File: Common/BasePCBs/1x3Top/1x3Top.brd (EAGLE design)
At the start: 100 x 80 mm, 1 part

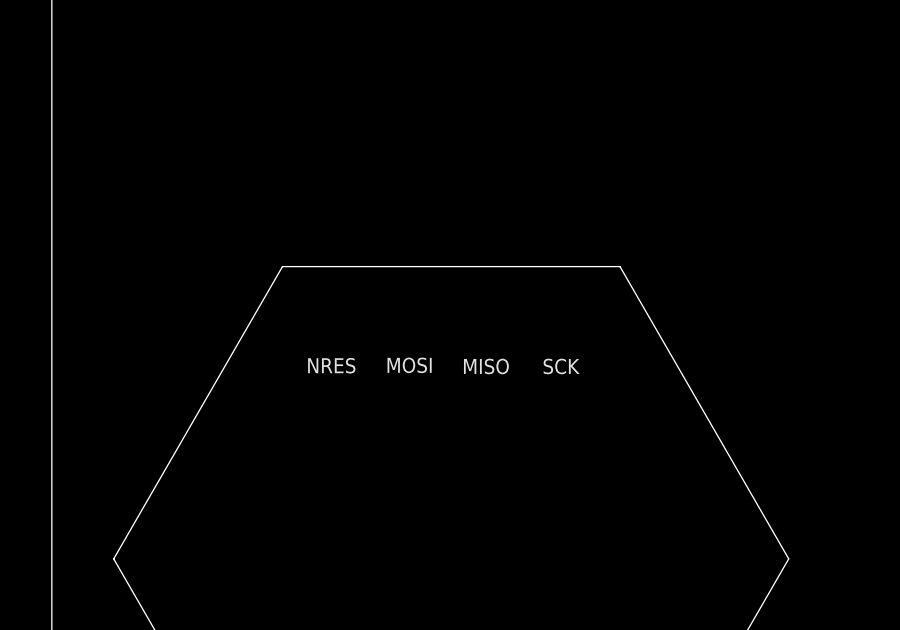
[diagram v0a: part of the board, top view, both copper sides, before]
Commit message: re-organized dimensions
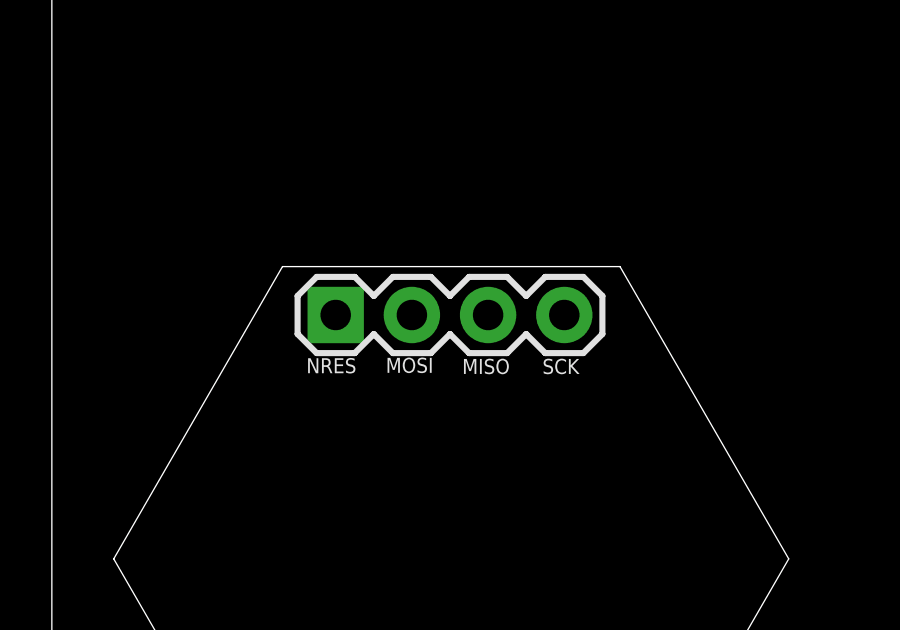
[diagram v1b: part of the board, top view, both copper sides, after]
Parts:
- added JP2: (no value), SparkFun-Connectors:1X04
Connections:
- new net 1X3SIN-SOUT: JP1.1, JP1.4
- new net MOSI: JP2.2
- new net NRES: JP2.1
- new net OUT(MISO): JP2.3
- new net SCK: JP2.4
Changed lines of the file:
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@@
 <attribute name="VALUE" x="18.4023" y="7.0739" size="1.27" layer="27" rot="R180"/>
+</element>
+<element name="JP2" library="SparkFun-Connectors" package="1X04" value="" x="9.4615" y="20.1676" smashed="yes">
+<attribute name="VALUE" x="8.1915" y="16.9926" size="1.27" layer="27"/>
 </element>
 </elements>
@@
 <contactref element="JP1" pad="2"/>
 </signal>
+<signal name="1X3SIN-SOUT">
+<contactref element="JP1" pad="4"/>
+<contactref element="JP1" pad="1"/>
+<wire x1="9.5123" y1="3.8989" x2="17.1323" y2="3.8989" width="0" layer="19" extent="1-1"/>
+</signal>
+<signal name="NRES">
+<contactref element="JP2" pad="1"/>
+</signal>
+<signal name="MOSI">
+<contactref element="JP2" pad="2"/>
+</signal>
+<signal name="SCK">
+<contactref element="JP2" pad="4"/>
+</signal>
+<signal name="OUT(MISO)">
+<contactref element="JP2" pad="3"/>
+</signal>
 </signals>

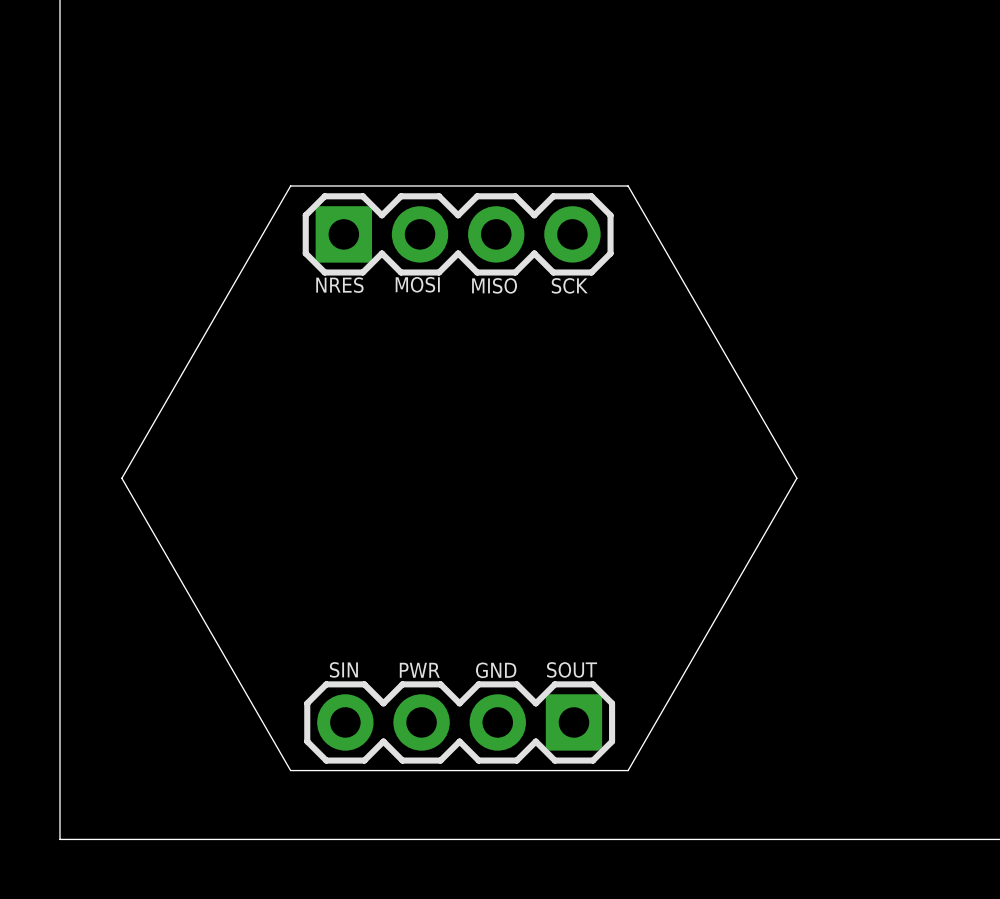
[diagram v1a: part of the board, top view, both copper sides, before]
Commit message: Added programmable module's top PCB
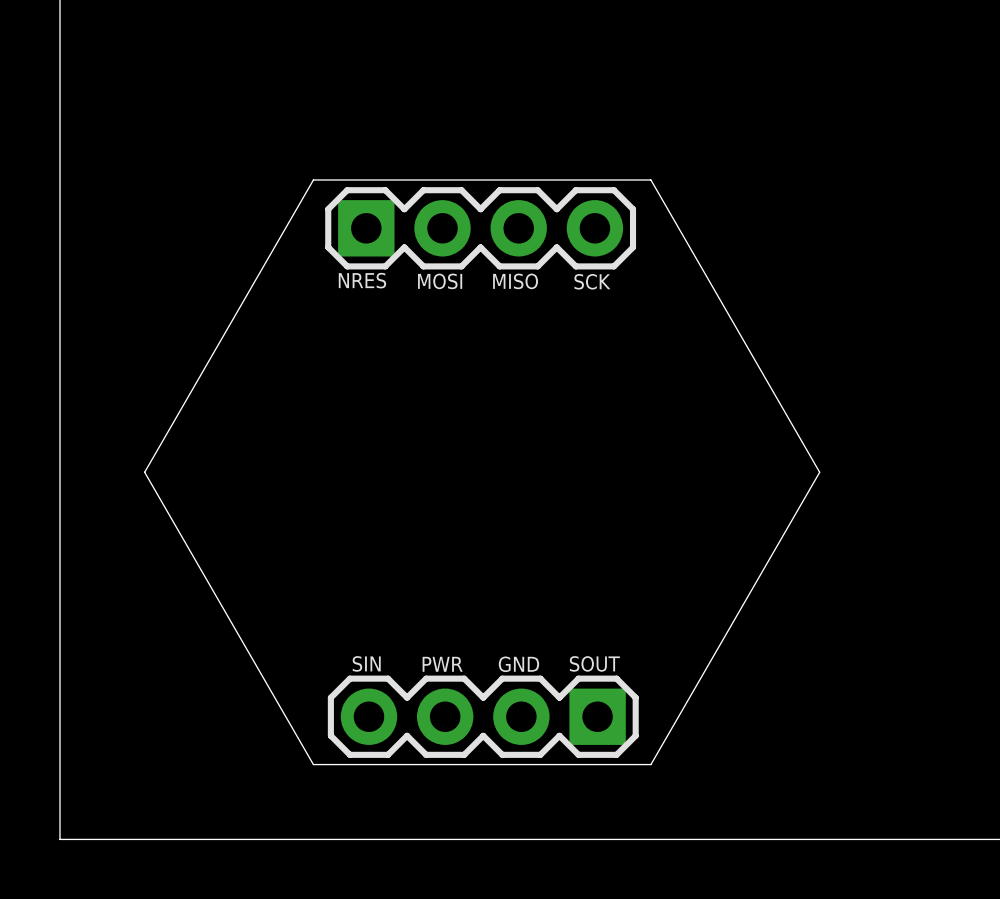
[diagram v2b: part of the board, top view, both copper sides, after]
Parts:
- moved JP1 0.81 mm to (17.9, 4.09)
- moved JP2 0.78 mm to (10.2, 20.4)
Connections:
- removed net 1X3SIN-SOUT: JP1.1, JP1.4
- new net 1X3SIN: JP1.4
- new net 1X3SOUT: JP1.1
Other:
- outline, holes or cut-outs redrawn
